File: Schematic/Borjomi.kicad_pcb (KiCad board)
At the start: 2 copper layers, 10 parts, among them J1 Vin 12V, J2 Vout 12V, J3 Water Switch 12V, J4 Data in, J5 Data out, J6 Conn_01x02, U1 MCP2515-TJA1050, U2 MH-Series, U3 5V_Relay_Module

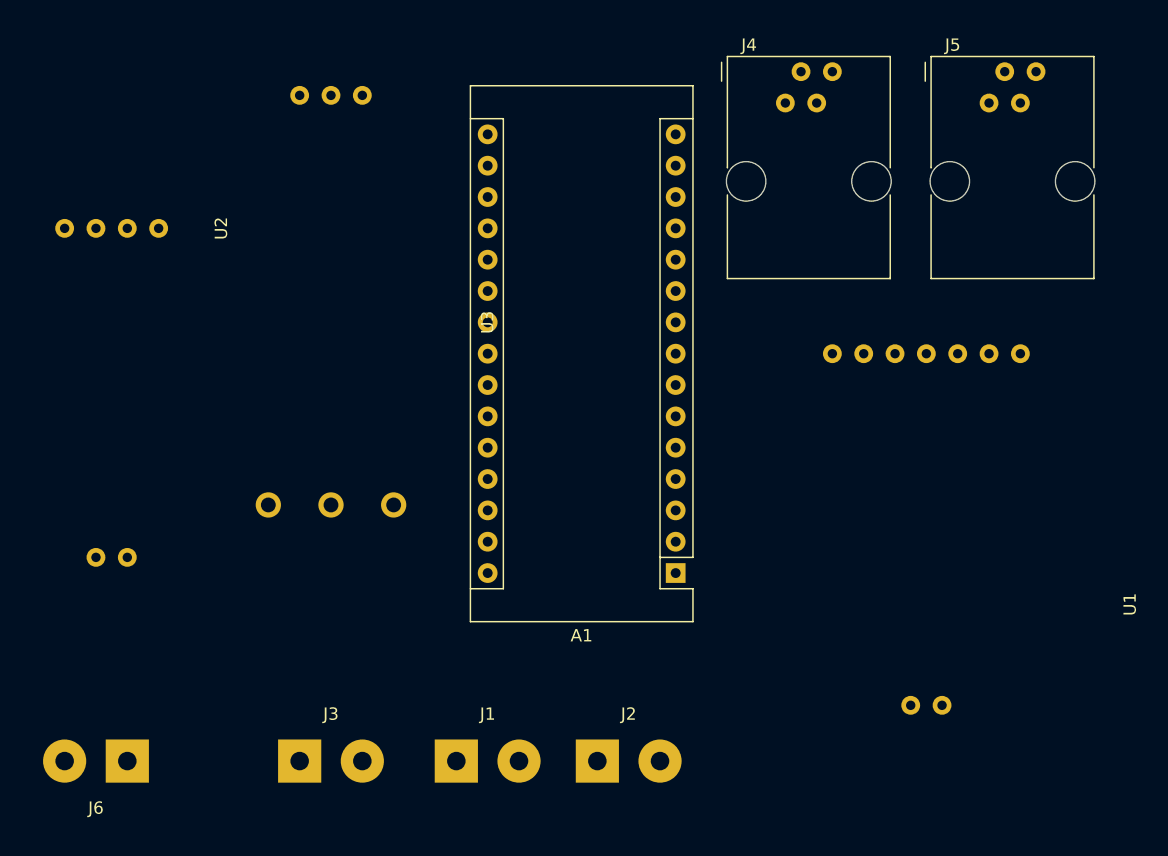
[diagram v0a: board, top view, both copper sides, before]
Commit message: Update footprints (place pads in right order)
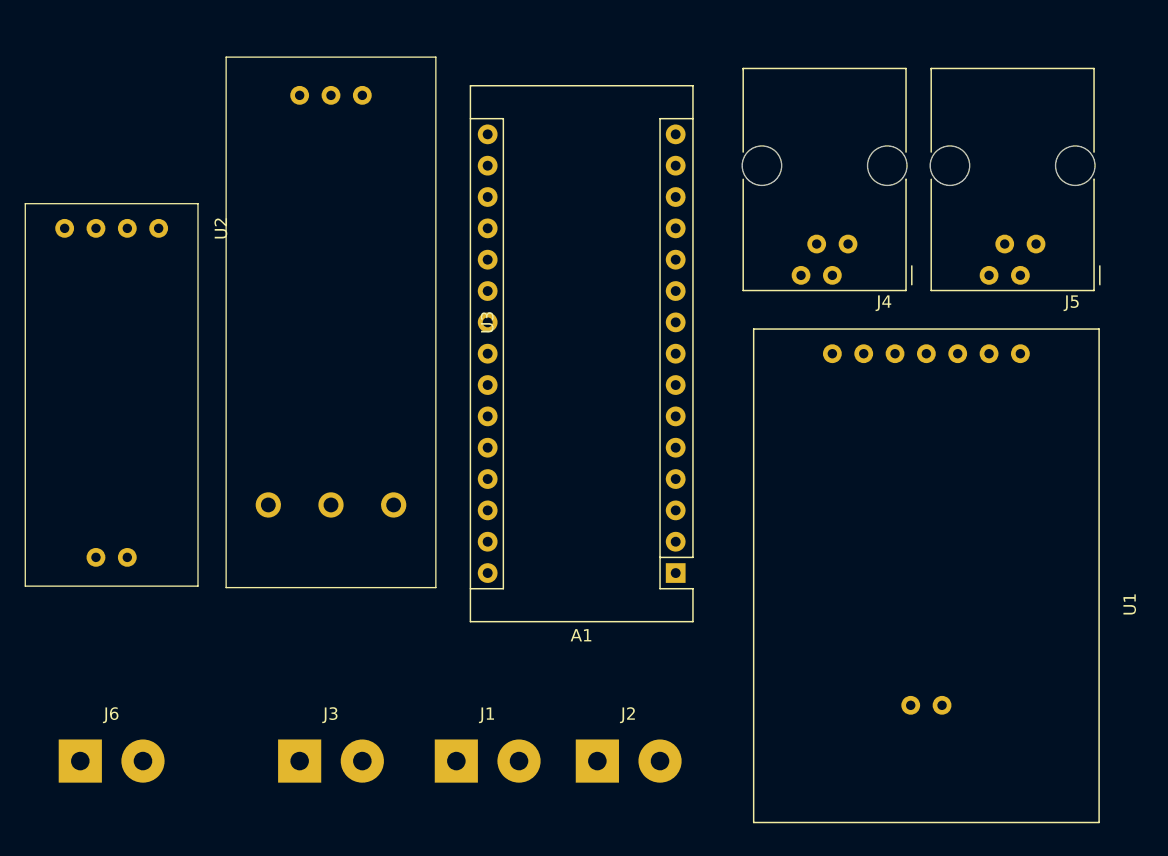
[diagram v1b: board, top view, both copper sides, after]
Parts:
- moved J4 18.2 mm to (111.8, 54.6), turned to 180 degrees
- moved J5 17.7 mm to (127.0, 54.6), turned to 180 degrees
- moved J6 3.81 mm to (48.3, 94.0), turned to 0 degrees
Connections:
- U2 pad 5: Net-(J6-Pad1) -> Net-(J6-Pad2)
- U2 pad 6: Net-(J6-Pad2) -> Net-(J6-Pad1)
- U3 pad 4: (no net) -> Net-(J3-Pad1)
- U3 pad 6: Net-(J3-Pad1) -> (no net)

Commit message: Pcb v1.0 + gerber files
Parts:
- added D1: 1N5408, Diode_THT:D_DO-27_P5.08mm_Vertical_KathodeUp, F.Cu at (67.5, 50.8)
- J1, J2, J3, J6: footprint Connector_Wire:SolderWirePad_1x02_P5.08mm_Drill1.5mm -> Connector:Degson_DG301_1x02_P5.00mm_Horizontal
- moved J1 53.8 mm to (92.5, 41.9), turned to 180 degrees
- moved J6 53.2 mm to (59.1, 41.9), turned to 180 degrees
- moved J2 52.6 mm to (82.5, 41.9), turned to 180 degrees
- moved J3 52.5 mm to (72.5, 41.9), turned to 180 degrees
- moved U2 40.4 mm to (56.5, 90.8), turned to 90 degrees
- moved U1 34.3 mm to (115.6, 95.2), turned to 90 degrees
- moved A1 26.5 mm to (83.2, 55.9), turned to 0 degrees
- moved U3 18.2 mm to (72.4, 76.2), turned to 90 degrees
- moved J5 15.9 mm to (111.1, 54.6)
- moved J4 14.6 mm to (126.4, 54.6)
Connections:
- A1 pad 5: Net-(A1-Pad5) -> (no net)
- A1 pad 8: (no net) -> Net-(A1-Pad8)
- J3 pad 1: Net-(J3-Pad1) -> GND
- J3 pad 2: GND -> Net-(D1-Pad1)
- U1 pad 1: Net-(J4-Pad2) -> Net-(J4-Pad1)
- U1 pad 2: Net-(J4-Pad1) -> Net-(J4-Pad2)
- U1 pad 3: Net-(A1-Pad5) -> Net-(A1-Pad8)
- U2 pad 5: Net-(J6-Pad2) -> Net-(J6-Pad1)
- U2 pad 6: Net-(J6-Pad1) -> Net-(J6-Pad2)
- U3 pad 4: Net-(J3-Pad1) -> +12V
- U3 pad 5: +12V -> Net-(D1-Pad1)
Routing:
- net Net-(A1-Pad27): track 0.00 -> 108.3 mm
- net Net-(A1-Pad19): track 0.00 -> 76.4 mm
- net +12V: track 0.00 -> 50.3 mm
- net Net-(A1-Pad8): track 0.00 -> 46.2 mm
- net GND: track 0.00 -> 44.2 mm
- net Net-(A1-Pad12): track 0.00 -> 39.7 mm
- net Net-(J4-Pad1): track 0.00 -> 35.0 mm
- net Net-(A1-Pad15): track 0.00 -> 35.0 mm
- net Net-(A1-Pad14): track 0.00 -> 32.5 mm
- net Net-(J4-Pad2): track 0.00 -> 32.4 mm
- net Net-(A1-Pad6): track 0.00 -> 29.4 mm
- net Net-(J6-Pad1): track 0.00 -> 23.4 mm
- net Net-(J6-Pad2): track 0.00 -> 22.7 mm
- net Net-(D1-Pad1): track 0.00 -> 22.6 mm
- net Net-(J4-Pad3): track 0.00 -> 16.3 mm
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- added copper zone on B.Cu, net (none)
- added copper zone on B.Cu, net GND
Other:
- board outline added: 81.9 x 64.1 mm
- board text added: "+"
- board text added: "12V IN"
- board text added: "12V OUT"
- board text added: "Borjomi v1.0"
- board text added: "Data IN"
- board text added: "Data OUT"
- board text added: "Soil Moisture"
- board text added: "Switch"

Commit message: PCB v1.1 + gerber
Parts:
- A1: footprint Module:Arduino_Nano -> Arduino:Arduino_Nano_Holes0.9
- U1: footprint CAN:AOC346_MCP2515 -> CAN:AOC346_MCP2515_Holes0.9
- U2: footprint MH_Sensor:MH_Sensor -> MH_Sensor:MH_Sensor_Holes0.9
- U3: footprint RelayModule:Relay_Module_1_Channel -> RelayModule:Relay_Module_1_Channel_Holes0.9
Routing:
- net GND: track 44.2 -> 34.2 mm
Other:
- board text added: "Borjomi v1.1"
- board text removed: "Borjomi v1.0"
